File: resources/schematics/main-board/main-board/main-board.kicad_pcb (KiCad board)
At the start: 2 copper layers, 53.3 x 30.5 mm, 6 parts, among them J1 Conn_01x02_Female, J2 Conn_01x04_Female, J3 Conn_01x03_Female

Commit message: Refactor PCB - batch-20201231
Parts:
- added R3: 10K, Resistor_THT:R_Axial_DIN0309_L9.0mm_D3.2mm_P12.70mm_Horizontal, B.Cu at (77.5, 96.7)
- added R4: 10K, Resistor_THT:R_Axial_DIN0309_L9.0mm_D3.2mm_P12.70mm_Horizontal, B.Cu at (81.8, 96.7)
- added SW1: SW_Push_DPDT, clvlabs:Switch_DPDT_7x7mm, F.Cu at (87.6, 83.8)
- added SW2: SW_Push_45deg, Button_Switch_THT:SW_PUSH_6mm_H7.3mm, F.Cu at (87.9, 62.7)
- added SW3: SW_Push_45deg, Button_Switch_THT:SW_PUSH_6mm_H7.3mm, F.Cu at (87.9, 73.4)
- A1, R1, R2: moved to B.Cu
- J1: footprint Connector_PinSocket_2.54mm:PinSocket_1x02_P2.54mm_Vertical -> digikey-footprints:PinHeader_1x2_P2.54mm_Drill1.02mm
- J2: footprint Connector_PinSocket_2.54mm:PinSocket_1x04_P2.54mm_Vertical -> digikey-footprints:PinHeader_1x4_P2.54mm_Drill1.02mm
- J3: value Conn_01x03_Female -> Conn_01x04_Female; footprint Connector_PinSocket_2.54mm:PinSocket_1x03_P2.54mm_Vertical -> digikey-footprints:PinHeader_1x4_P2.54mm_Drill1.02mm
- moved J2 70.6 mm to (65.0, 54.1), turned to 0 degrees
- moved A1 58.6 mm to (73.7, 61.0), turned to 180 degrees
- moved J3 53.7 mm to (55.2, 83.8)
- moved R1 49.0 mm to (77.5, 68.1), turned to 90 degrees
- moved J1 45.4 mm to (86.9, 94.5), turned to 0 degrees
- moved R2 43.6 mm to (81.3, 68.1), turned to 90 degrees
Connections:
- net DISTANCE_SENSOR_PIN renamed PING_TRIGGER_PIN
- A1 pad 20: Net-(A1-Pad20) -> PING_ECHO_PIN
- A1 pad 6: Net-(A1-Pad6) -> BUTTON_UP_PIN
- A1 pad 7: Net-(A1-Pad7) -> BUTTON_DOWN_PIN
- J1 pad 1: GND -> BATT_GND
- J1 pad 2: VIN -> BATT_VIN
- J2 pad 1: GND -> +5V
- J2 pad 2: +5V -> GND
- J3 pad 2: +5V -> PING_ECHO_PIN
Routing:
- net +5V: track 33.9 -> 94.6 mm
- net VIN: track 5.08 -> 54.3 mm
- net BUTTON_UP_PIN: track 0.00 -> 38.1 mm
- net I2C_SDA: track 11.2 -> 41.8 mm
- net BUTTON_DOWN_PIN: track 0.00 -> 27.5 mm
- net I2C_SCL: track 18.8 -> 45.2 mm
- net BATT_VIN: track 0.00 -> 8.00 mm
- net BATT_GND: track 0.00 -> 6.98 mm
- net PING_ECHO_PIN: track 0.00 -> 3.26 mm
- net PING_TRIGGER_PIN: track 5.08 -> 3.26 mm
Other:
- board size 53.3 x 30.5 mm -> 50 x 50 mm
- board text added: "20201231"
- board text added: "Arduino Nano"
- board text added: "github.com/clvLabs/gas-oil-tank-level"

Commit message: Add horizontal pin header for connector
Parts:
- J3: footprint digikey-footprints:PinHeader_1x4_P2.54mm_Drill1.02mm -> Connector_PinHeader_2.54mm:PinHeader_1x04_P2.54mm_Horizontal
- moved J3 7.61 mm to (55.2, 91.4), turned to 180 degrees
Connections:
- J3 pad 1: GND -> +5V
- J3 pad 2: PING_ECHO_PIN -> PING_TRIGGER_PIN
- J3 pad 3: PING_TRIGGER_PIN -> PING_ECHO_PIN
- J3 pad 4: +5V -> GND
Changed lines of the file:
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@@
     (add_net VIN)
+  )
+  (module Connector_PinHeader_2.54mm:PinHeader_1x04_P2.54mm_Horizontal (layer F.Cu)
+    (at 55.159582 91.44 180)
+    (descr "Through hole angled pin header, 1x04, 2.54mm pitch, 6mm pin length, single row")
+    (tags "Through hole angled pin header THT 1x04 2.54mm single row")
+    (fp_text reference J3 (at 10.16 0 180) (layer F.SilkS)
+      (effects (font (size 1 1) (thickness 0.15)))
+    )
+    (fp_text value Conn_01x04_Female (at 4.08 4.52) (layer F.Fab)
+      (effects (font (size 1 1) (thickness 0.15)))
+    )
+    (fp_line (start 10.55 -1.8) (end -1.8 -1.8) (layer F.CrtYd) (width 0.05))
+    (fp_line (start 10.55 9.4) (end 10.55 -1.8) (layer F.CrtYd) (width 0.05))
+    (fp_line (start -1.8 9.4) (end 10.55 9.4) (layer F.CrtYd) (width 0.05))
+    (fp_line (start -1.8 -1.8) (end -1.8 9.4) (layer F.CrtYd) (width 0.05))
+    (fp_line (start -1.27 -1.27) (end 0 -1.27) (layer F.SilkS) (width 0.12))
+    (fp_line (start -1.27 0) (end -1.27 -1.27) (layer F.SilkS) (width 0.12))
+    (fp_line (start 1.042929 8) (end 1.44 8) (layer F.SilkS) (width 0.12))
+    (fp_line (start 1.042929 7.24) (end 1.44 7.24) (layer F.SilkS) (width 0.12))
+    (fp_line (start 10.1 8) (end 4.1 8) (layer F.SilkS) (width 0.12))
+    (fp_line (start 10.1 7.24) (end 10.1 8) (layer F.SilkS) (width 0.12))
+    (fp_line (start 4.1 7.24) (end 10.1 7.24) (layer F.SilkS) (width 0.12))
+    (fp_line (start 1.44 6.35) (end 4.1 6.35) (layer F.SilkS) (width 0.12))
+    (fp_line (start 1.042929 5.46) (end 1.44 5.46) (layer F.SilkS) (width 0.12))
+    (fp_line (start 1.042929 4.7) (end 1.44 4.7) (layer F.SilkS) (width 0.12))
+    (fp_line (start 10.1 5.46) (end 4.1 5.46) (layer F.SilkS) (width 0.12))
+    (fp_line (start 10.1 4.7) (end 10.1 5.46) (layer F.SilkS) (width 0.12))
+    (fp_line (start 4.1 4.7) (end 10.1 4.7) (layer F.SilkS) (width 0.12))
+    (fp_line (start 1.44 3.81) (end 4.1 3.81) (layer F.SilkS) (width 0.12))
+    (fp_line (start 1.042929 2.92) (end 1.44 2.92) (layer F.SilkS) (width 0.12))
+    (fp_line (start 1.042929 2.16) (end 1.44 2.16) (layer F.SilkS) (width 0.12))
+    (fp_line (start 10.1 2.92) (end 4.1 2.92) (layer F.SilkS) (width 0.12))
+    (fp_line (start 10.1 2.16) (end 10.1 2.92) (layer F.SilkS) (width 0.12))
+    (fp_line (start 4.1 2.16) (end 10.1 2.16) (layer F.SilkS) (width 0.12))
+    (fp_line (start 1.44 1.27) (end 4.1 1.27) (layer F.SilkS) (width 0.12))
+    (fp_line (start 1.11 0.38) (end 1.44 0.38) (layer F.SilkS) (width 0.12))
+    (fp_line (start 1.11 -0.38) (end 1.44 -0.38) (layer F.SilkS) (width 0.12))
+    (fp_line (start 4.1 0.28) (end 10.1 0.28) (layer F.SilkS) (width 0.12))
+    (fp_line (start 4.1 0.16) (end 10.1 0.16) (layer F.SilkS) (width 0.12))
+    (fp_line (start 4.1 0.04) (end 10.1 0.04) (layer F.SilkS) (width 0.12))
+    (fp_line (start 4.1 -0.08) (end 10.1 -0.08) (layer F.SilkS) (width 0.12))
+    (fp_line (start 4.1 -0.2) (end 10.1 -0.2) (layer F.SilkS) (width 0.12))
+    (fp_line (start 4.1 -0.32) (end 10.1 -0.32) (layer F.SilkS) (width 0.12))
+    (fp_line (start 10.1 0.38) (end 4.1 0.38) (layer F.SilkS) (width 0.12))
+    (fp_line (start 10.1 -0.38) (end 10.1 0.38) (layer F.SilkS) (width 0.12))
+    (fp_line (start 4.1 -0.38) (end 10.1 -0.38) (layer F.SilkS) (width 0.12))
+    (fp_line (start 4.1 -1.33) (end 1.44 -1.33) (layer F.SilkS) (width 0.12))
+    (fp_line (start 4.1 8.95) (end 4.1 -1.33) (layer F.SilkS) (width 0.12))
+    (fp_line (start 1.44 8.95) (end 4.1 8.95) (layer F.SilkS) (width 0.12))
+    (fp_line (start 1.44 -1.33) (end 1.44 8.95) (layer F.SilkS) (width 0.12))
+    (fp_line (start 4.04 7.94) (end 10.04 7.94) (layer F.Fab) (width 0.1))
+    (fp_line (start 10.04 7.3) (end 10.04 7.94) (layer F.Fab) (width 0.1))
+    (fp_line (start 4.04 7.3) (end 10.04 7.3) (layer F.Fab) (width 0.1))
+    (fp_line (start -0.32 7.94) (end 1.5 7.94) (layer F.Fab) (width 0.1))
+    (fp_line (start -0.32 7.3) (end -0.32 7.94) (layer F.Fab) (width 0.1))
+    (fp_line (start -0.32 7.3) (end 1.5 7.3) (layer F.Fab) (width 0.1))
+    (fp_line (start 4.04 5.4) (end 10.04 5.4) (layer F.Fab) (width 0.1))
+    (fp_line (start 10.04 4.76) (end 10.04 5.4) (layer F.Fab) (width 0.1))
+    (fp_line (start 4.04 4.76) (end 10.04 4.76) (layer F.Fab) (width 0.1))
+    (fp_line (start -0.32 5.4) (end 1.5 5.4) (layer F.Fab) (width 0.1))
+    (fp_line (start -0.32 4.76) (end -0.32 5.4) (layer F.Fab) (width 0.1))
+    (fp_line (start -0.32 4.76) (end 1.5 4.76) (layer F.Fab) (width 0.1))
+    (fp_line (start 4.04 2.86) (end 10.04 2.86) (layer F.Fab) (width 0.1))
+    (fp_line (start 10.04 2.22) (end 10.04 2.86) (layer F.Fab) (width 0.1))
+    (fp_line (start 4.04 2.22) (end 10.04 2.22) (layer F.Fab) (width 0.1))
+    (fp_line (start -0.32 2.86) (end 1.5 2.86) (layer F.Fab) (width 0.1))
+    (fp_line (start -0.32 2.22) (end -0.32 2.86) (layer F.Fab) (width 0.1))
+    (fp_line (start -0.32 2.22) (end 1.5 2.22) (layer F.Fab) (width 0.1))
+    (fp_line (start 4.04 0.32) (end 10.04 0.32) (layer F.Fab) (width 0.1))
+    (fp_line (start 10.04 -0.32) (end 10.04 0.32) (layer F.Fab) (width 0.1))
+    (fp_line (start 4.04 -0.32) (end 10.04 -0.32) (layer F.Fab) (width 0.1))
+    (fp_line (start -0.32 0.32) (end 1.5 0.32) (layer F.Fab) (width 0.1))
+    (fp_line (start -0.32 -0.32) (end -0.32 0.32) (layer F.Fab) (width 0.1))
+    (fp_line (start -0.32 -0.32) (end 1.5 -0.32) (layer F.Fab) (width 0.1))
+    (fp_line (start 1.5 -0.635) (end 2.135 -1.27) (layer F.Fab) (width 0.1))
+    (fp_line (start 1.5 8.89) (end 1.5 -0.635) (layer F.Fab) (width 0.1))
+    (fp_line (start 4.04 8.89) (end 1.5 8.89) (layer F.Fab) (width 0.1))
+    (fp_line (start 4.04 -1.27) (end 4.04 8.89) (layer F.Fab) (width 0.1))
+    (fp_line (start 2.135 -1.27) (end 4.04 -1.27) (layer F.Fab) (width 0.1))
+    (fp_text user %R (at 4.17 0) (layer F.Fab)
+      (effects (font (size 1 1) (thickness 0.15)))
+    )
+    (pad 4 thru_hole oval (at 0 7.62 180) (size 1.7 1.7) (drill 1) (layers *.Cu *.Mask)
+      (net 6 GND))
+    (pad 3 thru_hole oval (at 0 5.08 180) (size 1.7 1.7) (drill 1) (layers *.Cu *.Mask)
+      (net 27 PING_ECHO_PIN))
+    (pad 2 thru_hole oval (at 0 2.54 180) (size 1.7 1.7) (drill 1) (layers *.Cu *.Mask)
+      (net 26 PING_TRIGGER_PIN))
+    (pad 1 thru_hole rect (at 0 0 180) (size 1.7 1.7) (drill 1) (layers *.Cu *.Mask)
+      (net 18 +5V))
+    (model ${KISYS3DMOD}/Connector_PinHeader_2.54mm.3dshapes/PinHeader_1x04_P2.54mm_Horizontal.wrl
+      (at (xyz 0 0 0))
+      (scale (xyz 1 1 1))
+      (rotate (xyz 0 0 0))
+    )
   )
   (module Module:Arduino_Nano (layer B.Cu)
@@
   )
   (module digikey-footprints:PinHeader_1x4_P2.54mm_Drill1.02mm (layer F.Cu)
-    (at 55.159582 83.827361 270)
-    (descr http://www.molex.com/pdm_docs/sd/022232031_sd.pdf)
-    (fp_text reference J3 (at 10.16 0 270) (layer F.SilkS)
-      (effects (font (size 1 1) (thickness 0.15)))
-    )
-    (fp_text value Conn_01x04_Female (at 4.08 4.52 90) (layer F.Fab)
-      (effects (font (size 1 1) (thickness 0.15)))
-    )
-    (fp_line (start 9.06 -3.42) (end 9.06 3.42) (layer F.CrtYd) (width 0.05))
-    (fp_line (start 8.81 -3.17) (end 8.81 3.17) (layer F.Fab) (width 0.1))
-    (fp_line (start -1.2 3.17) (end 8.81 3.17) (layer F.Fab) (width 0.1))
-    (fp_line (start 9.06 3.42) (end -1.45 3.42) (layer F.CrtYd) (width 0.05))
-    (fp_line (start -1.45 -3.42) (end -1.45 3.42) (layer F.CrtYd) (width 0.05))
-    (fp_line (start 9.06 -3.42) (end -1.45 -3.42) (layer F.CrtYd) (width 0.05))
-    (fp_line (start -1.3 -3.3) (end -1.3 -2.8) (layer F.SilkS) (width 0.1))
-    (fp_line (start -1.3 -3.3) (end -0.8 -3.3) (layer F.SilkS) (width 0.1))
-    (fp_line (start -1.3 3.3) (end -1.3 2.8) (layer F.SilkS) (width 0.1))
-    (fp_line (start -1.3 3.3) (end -0.8 3.3) (layer F.SilkS) (width 0.1))
-    (fp_line (start -1.2 -3.17) (end -1.2 3.17) (layer F.Fab) (width 0.1))
-    (fp_line (start -1.2 -3.17) (end 8.81 -3.17) (layer F.Fab) (width 0.1))
-    (fp_text user %R (at 4.17 0 90) (layer F.Fab)
-      (effects (font (size 1 1) (thickness 0.15)))
-    )
-    (pad 4 thru_hole circle (at 7.62 0 270) (size 2.02 2.02) (drill 1.02) (layers *.Cu *.Mask)
-      (net 18 +5V))
-    (pad 3 thru_hole circle (at 5.08 0 270) (size 2.02 2.02) (drill 1.02) (layers *.Cu *.Mask)
-      (net 26 PING_TRIGGER_PIN))
-    (pad 2 thru_hole circle (at 2.54 0 270) (size 2.02 2.02) (drill 1.02) (layers *.Cu *.Mask)
-      (net 27 PING_ECHO_PIN))
-    (pad 1 thru_hole circle (at 0 0 270) (size 2.02 2.02) (drill 1.02) (layers *.Cu *.Mask)
-      (net 6 GND))
-  )
-  (module digikey-footprints:PinHeader_1x4_P2.54mm_Drill1.02mm (layer F.Cu)

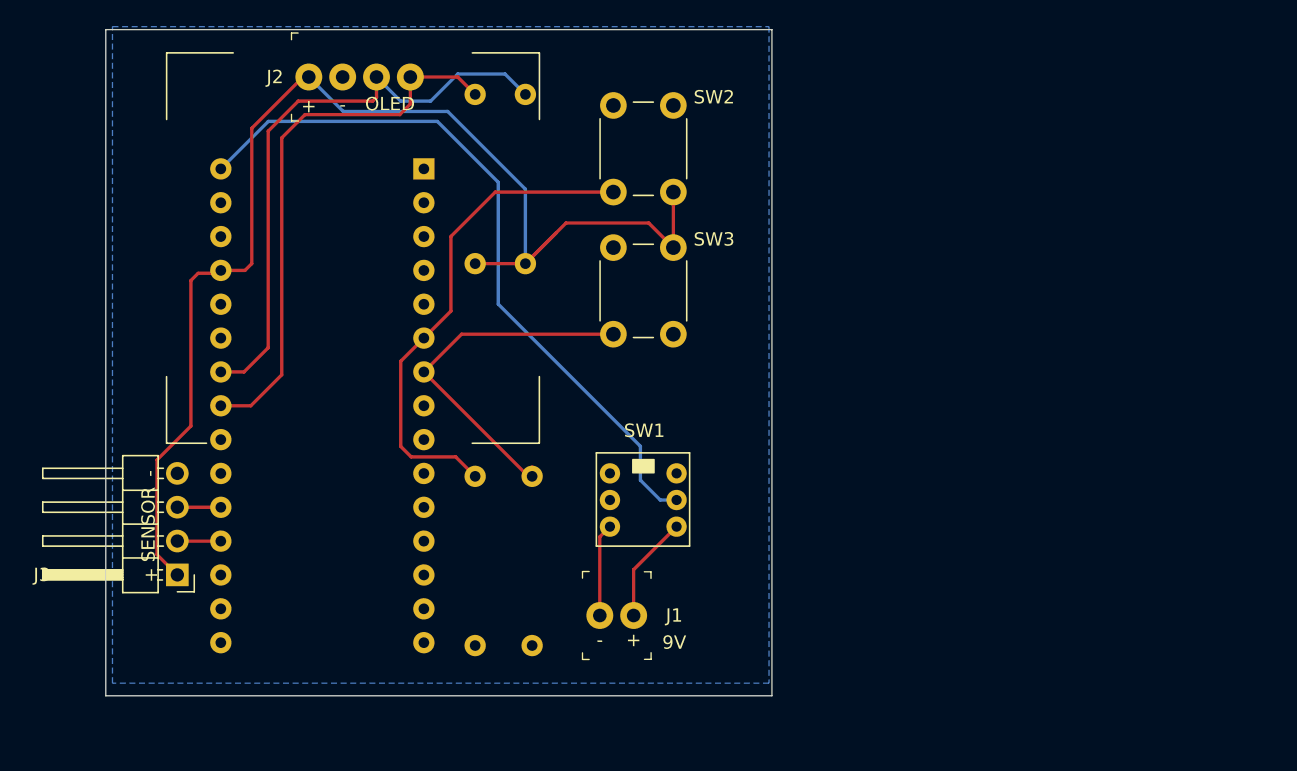
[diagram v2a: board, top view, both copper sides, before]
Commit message: Update footprints
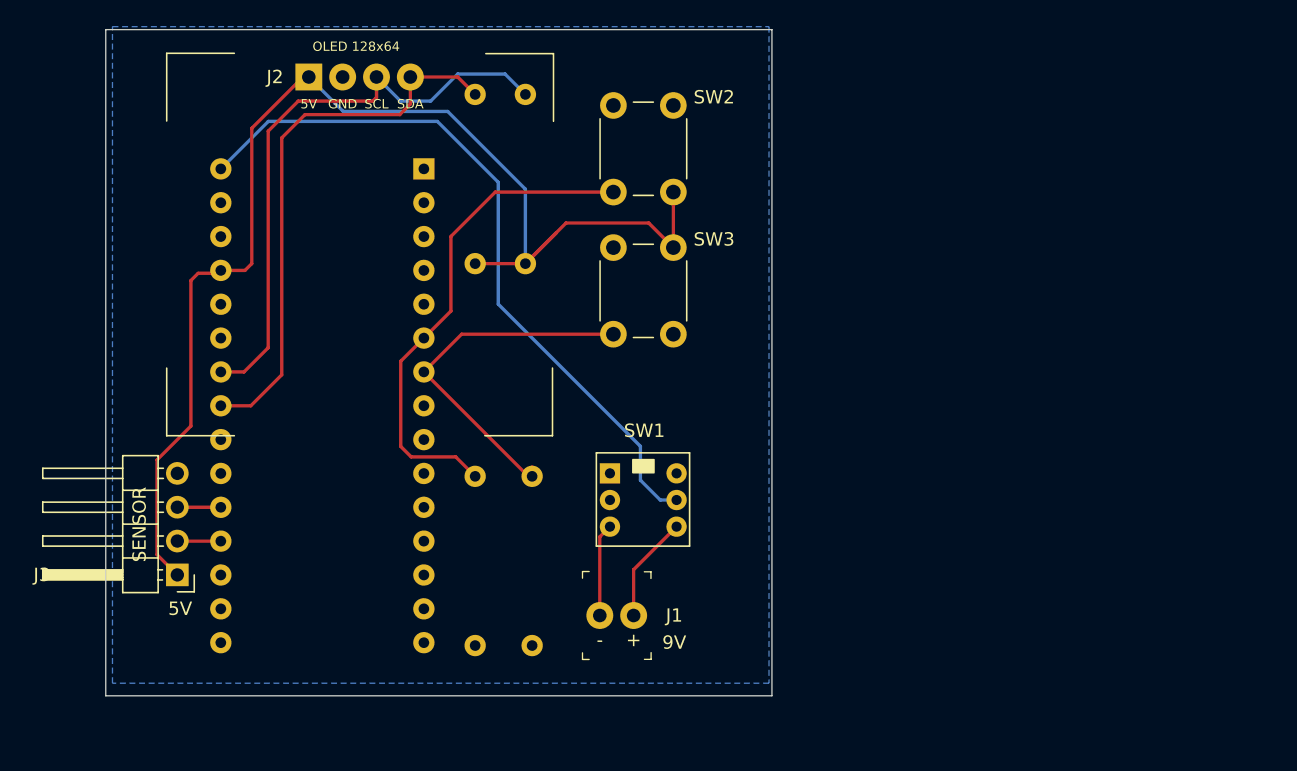
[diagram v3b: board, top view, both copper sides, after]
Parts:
- J2: footprint digikey-footprints:PinHeader_1x4_P2.54mm_Drill1.02mm -> clvlabs:OLED_128X64
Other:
- board text added: "5V"
- board text added: "yyyymmdd"
- board text removed: "20201231"
- board text removed: "OLED"
